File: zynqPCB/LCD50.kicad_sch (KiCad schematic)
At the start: 29 parts, among them J9 HDMI_A, Q10 IRLML2502, Q8 IRLML2502, Q9 IRLML2502, U20B xc7z020clg484, U20D xc7z020clg484, U20E xc7z020clg484, U21 PCA9306

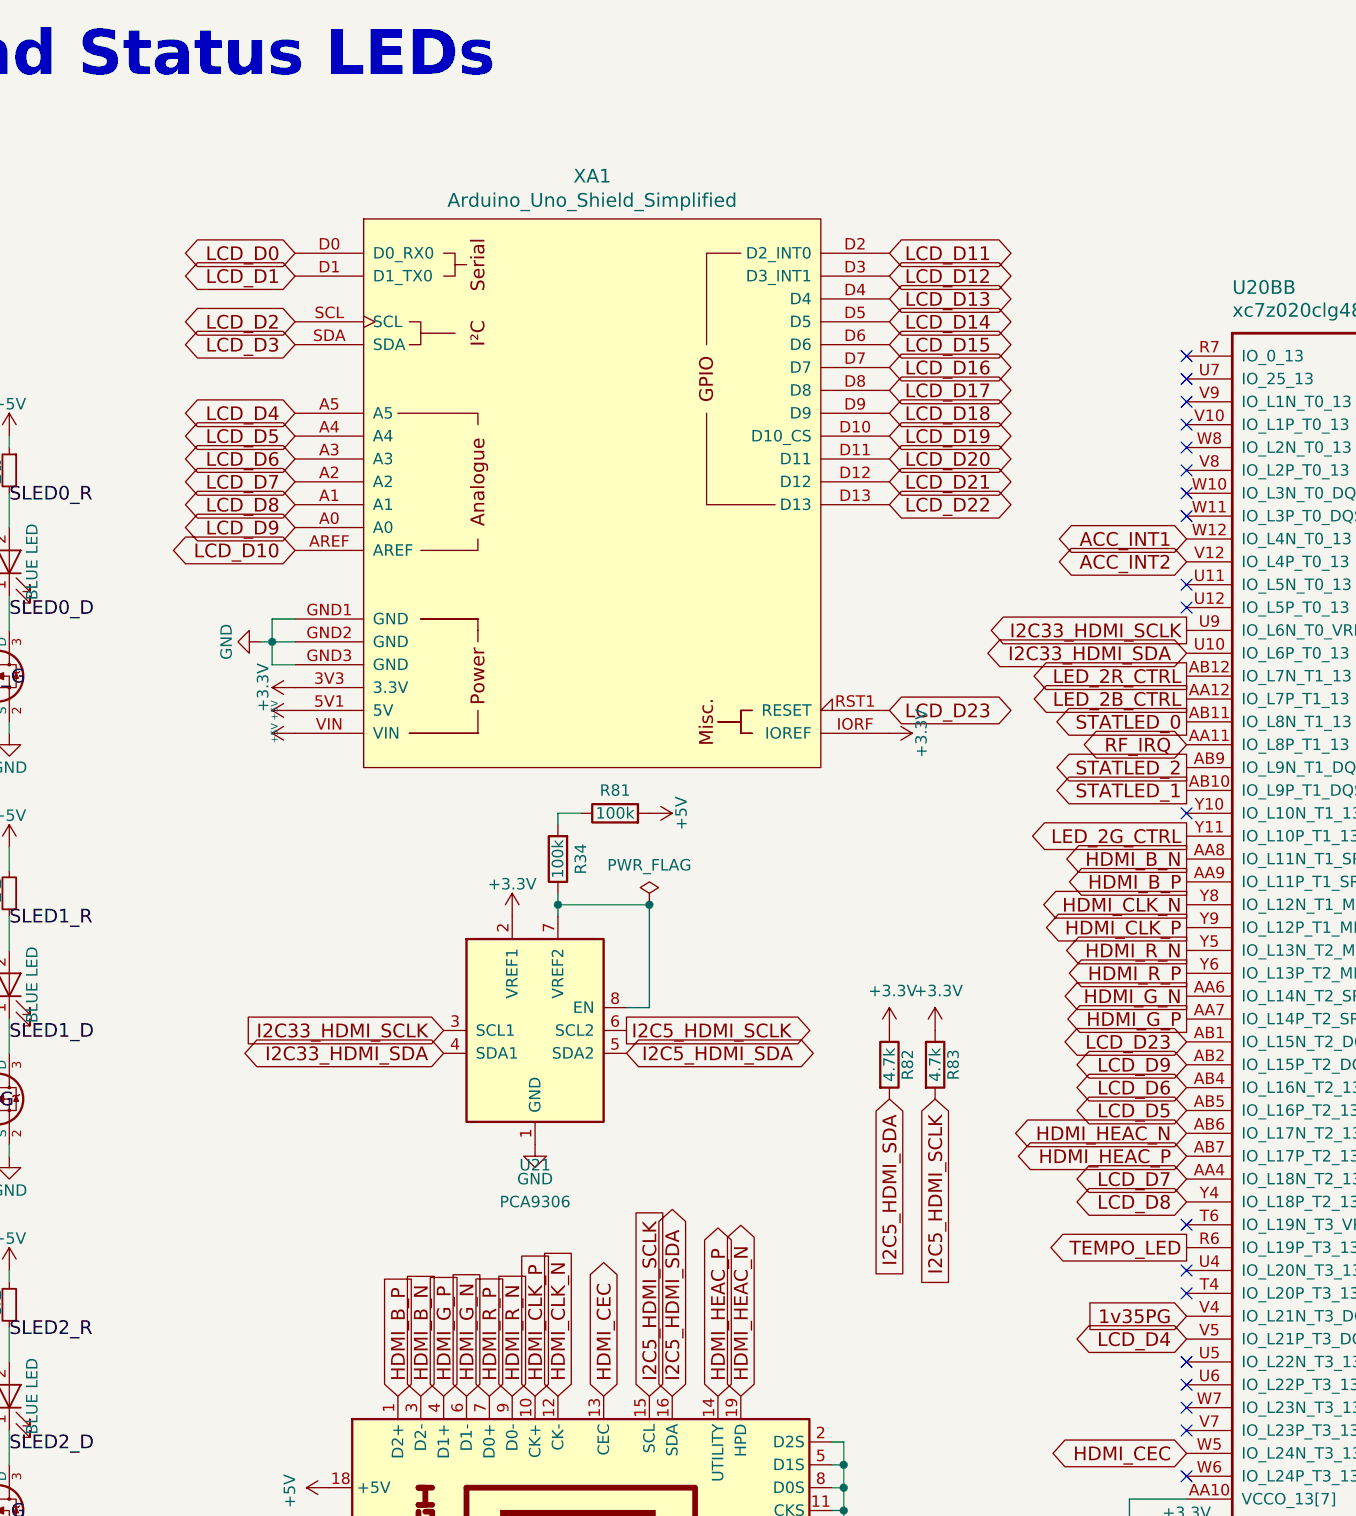
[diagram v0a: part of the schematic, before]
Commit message: Remove Sensors
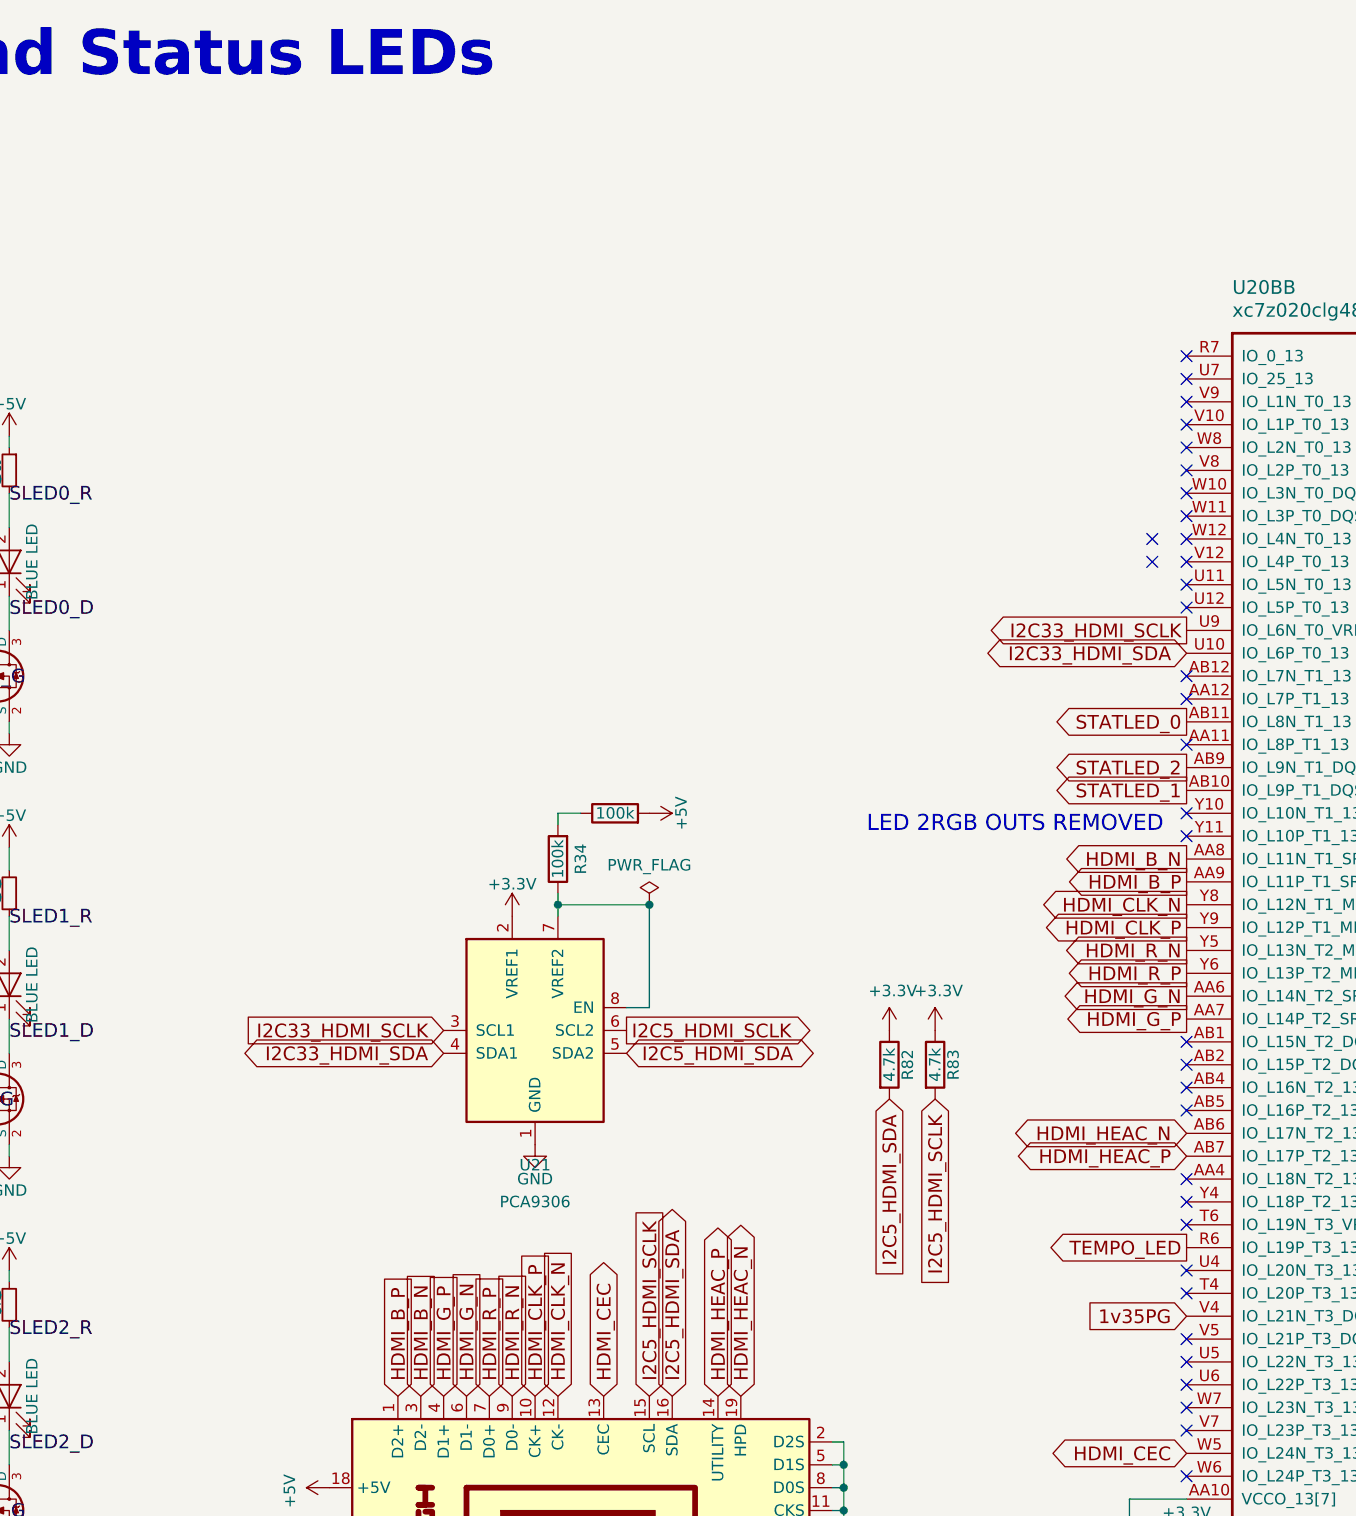
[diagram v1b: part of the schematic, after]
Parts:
- removed XA1: Arduino_Uno_Shield_Simplified, DFTcustom:Arduino_Uno_Shield_Simplified, symbol arduino:Arduino_Uno_Shield_Simplified
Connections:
- net ACC_INT1: no longer names the net of U20B.W12 (IO_L4N_T0_13)
- net ACC_INT2: no longer names the net of U20B.V12 (IO_L4P_T0_13)
- net LCD_D23: no longer names the net of U20B.AB1 (IO_L15N_T2_DQS_13)
- net LCD_D4: no longer names the net of U20B.V5 (IO_L21P_T3_DQS_13)
- net LCD_D5: no longer names the net of U20B.AB5 (IO_L16P_T2_13)
- net LCD_D6: no longer names the net of U20B.AB4 (IO_L16N_T2_13)
- net LCD_D7: no longer names the net of U20B.AA4 (IO_L18N_T2_13)
- net LCD_D8: no longer names the net of U20B.Y4 (IO_L18P_T2_13)
- net LCD_D9: no longer names the net of U20B.AB2 (IO_L15P_T2_DQS_13)
- net LED_2B_CTRL: no longer names the net of U20B.AA12 (IO_L7P_T1_13)
- net LED_2G_CTRL: no longer names the net of U20B.Y11 (IO_L10P_T1_13)
- net LED_2R_CTRL: no longer names the net of U20B.AB12 (IO_L7N_T1_13)
- net RF_IRQ: no longer names the net of U20B.AA11 (IO_L8P_T1_13)
- no-connect marks 19 -> 34
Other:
- note added: "LED 2RGB OUTS REMOVED"

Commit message: fix
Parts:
- renumbered D5 to D?, D4 to D?, D6 to D?, J9 to J?, Q9 to Q?, Q8 to Q?, Q10 to Q?, R79 to R?, R77 to R?, R80 to R?, R78 to R?, R85 to R?, R86 to R?, R82 to R?, R83 to R?, R34 to R?, R81 to R?
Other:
- moved on the sheet: C113, C114, C115, C116, C117, C118, C119, U20BB, U20DD, U20EE
